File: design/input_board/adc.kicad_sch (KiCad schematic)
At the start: 8 parts, among them IC9 ADS8860IDGSR, U14 REF6050xDGK, U15 uA7805

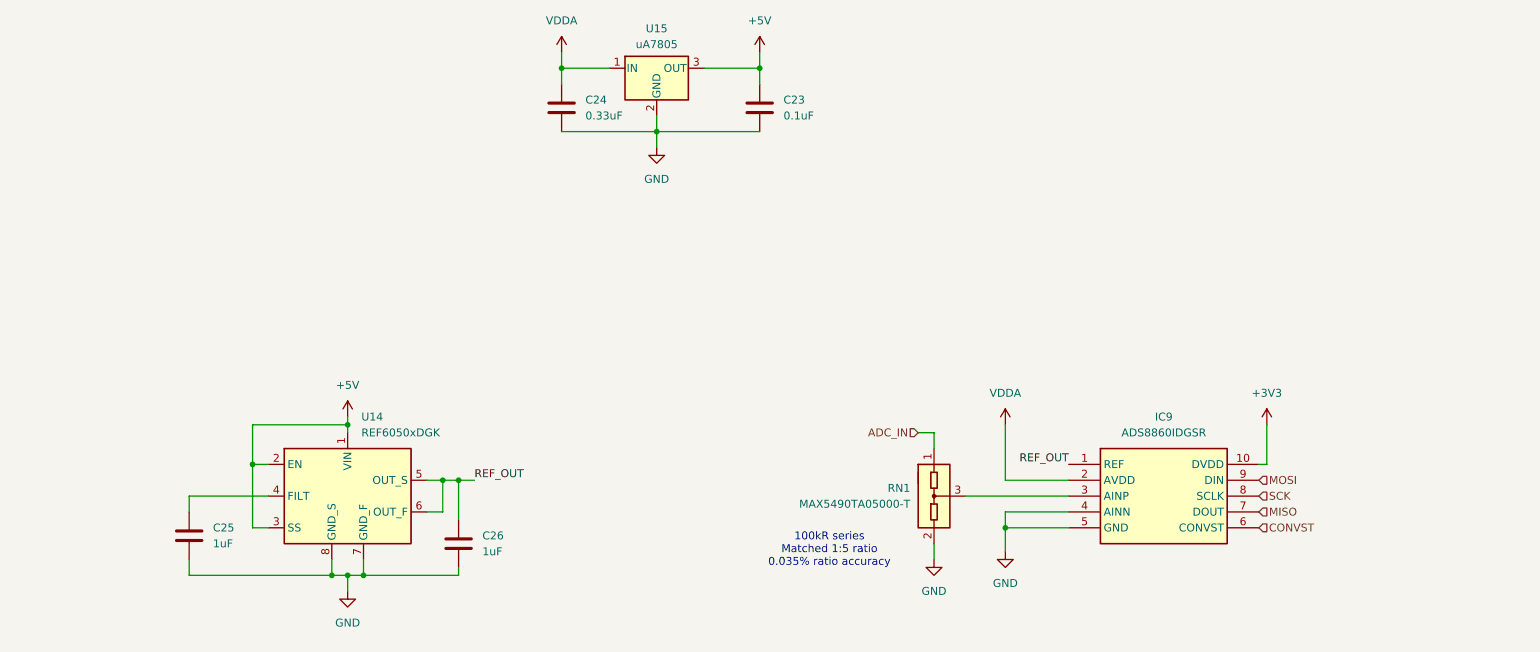
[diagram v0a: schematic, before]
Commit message: Finihs schamtic and footprints; DVDD 3.3->2V
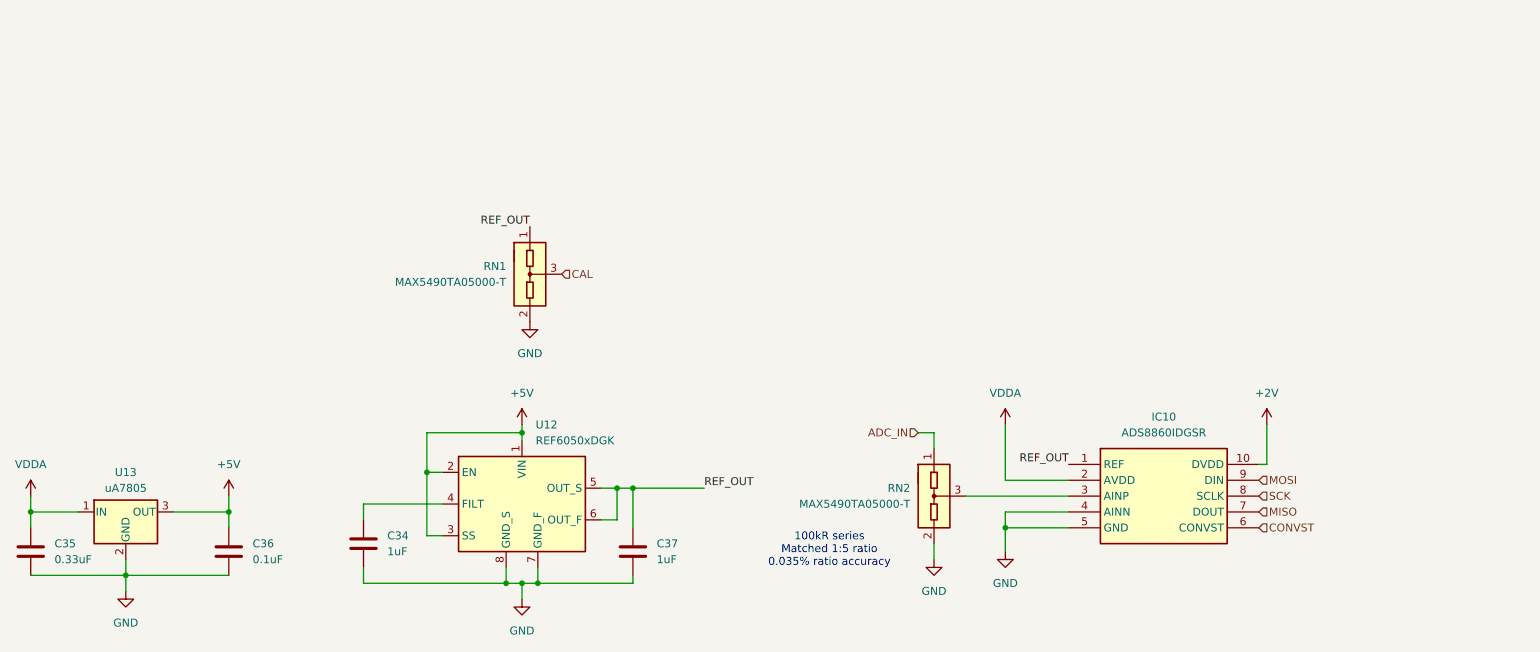
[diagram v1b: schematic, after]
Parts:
- added RN1: MAX5490TA05000-T, Package_TO_SOT_SMD:SOT-23, symbol input_board:MAX5490xxx-T
- C34: renamed from C25; footprint (none) -> Capacitor_SMD:C_0805_2012Metric_Pad1.18x1.45mm_HandSolder
- C35: renamed from C24; footprint (none) -> Capacitor_SMD:C_0805_2012Metric_Pad1.18x1.45mm_HandSolder
- C36: renamed from C23; footprint (none) -> Capacitor_SMD:C_0805_2012Metric_Pad1.18x1.45mm_HandSolder
- C37: renamed from C26; footprint (none) -> Capacitor_SMD:C_0805_2012Metric_Pad1.18x1.45mm_HandSolder
- U13: renamed from U15; footprint (none) -> Package_TO_SOT_SMD:TO-263-3_TabPin2
- renumbered IC9 to IC10, RN1 to RN2, U14 to U12
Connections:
- net GND: now also RN1.2 (R1)
- net REF_OUT: now also RN1.1 (COM1)
- net +3V3 renamed +2V
- new net CAL: RN1.3 (R2)
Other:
- moved on the sheet: C34, C35, C36, C37, U12, U13

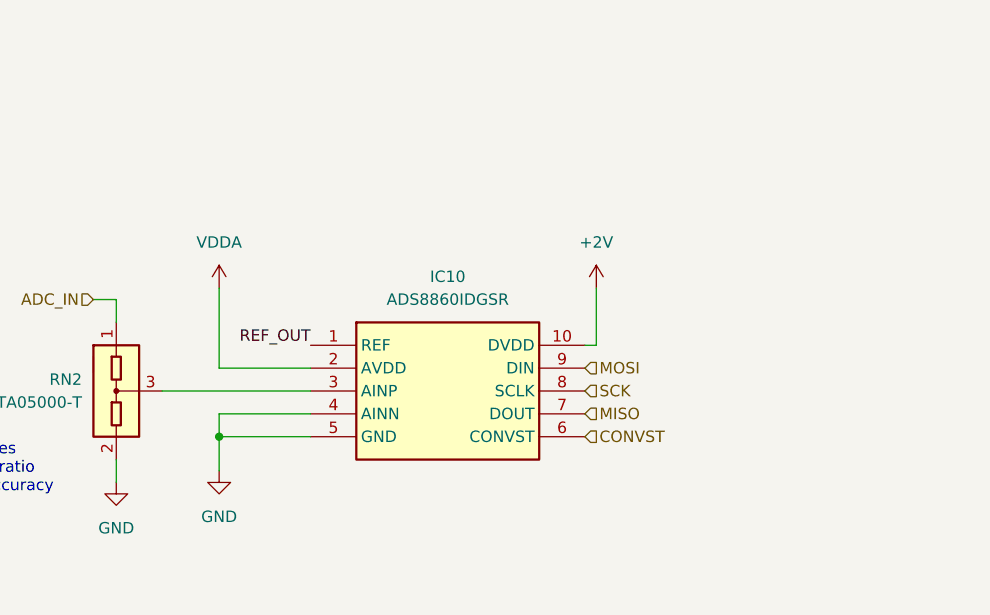
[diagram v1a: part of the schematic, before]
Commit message: Layout v1, its bad
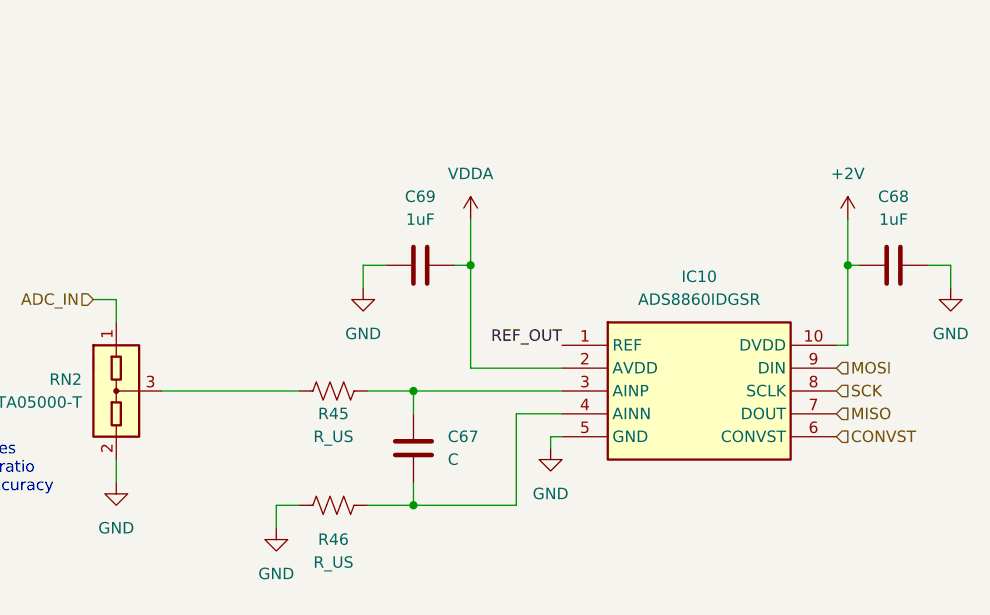
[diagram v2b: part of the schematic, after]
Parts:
- added C67: C, Capacitor_SMD:C_0805_2012Metric_Pad1.18x1.45mm_HandSolder, symbol Device:C
- added C68, C69: 1uF, Capacitor_SMD:C_0805_2012Metric_Pad1.18x1.45mm_HandSolder, symbol Device:C
- added R45, R46: R_US, Resistor_SMD:R_0805_2012Metric_Pad1.20x1.40mm_HandSolder, symbol Device:R_US
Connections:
- net +2V: now also C68.2
- net GND: now also C68.1, C69.1, R46.2; no longer IC10.4 (AINN)
- net VDDA: now also C69.2
- net at RN2.3 (R2): now also R45.1; no longer IC10.3 (AINP)
- new net: C67.2, IC10.3 (AINP), R45.2
- new net: C67.1, IC10.4 (AINN), R46.1
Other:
- moved on the sheet: IC10

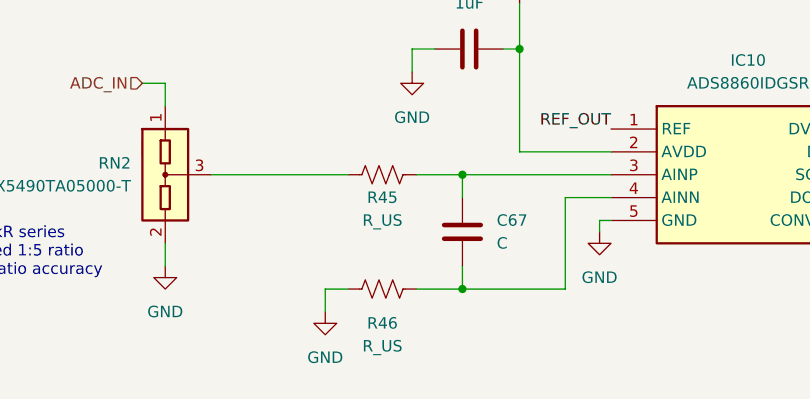
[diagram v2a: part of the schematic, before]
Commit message: Add values for charge bucket filter
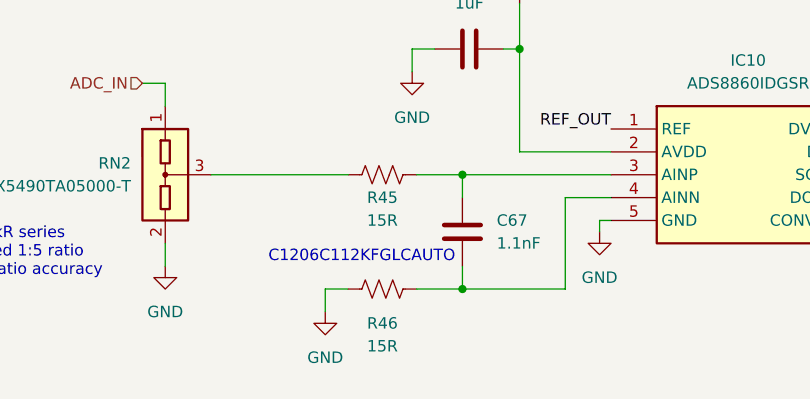
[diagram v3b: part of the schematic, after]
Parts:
- C67: value C -> 1.1nF
- R45, R46: value R_US -> 15R
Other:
- note added: "C1206C112KFGLCAUTO"
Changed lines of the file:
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@@
+		)
+	)
+	(text "C1206C112KFGLCAUTO"
+		(exclude_from_sim no)
+		(at 195.834 114.554 0)
+		(effects
+			(font
+				(size 1.27 1.27)
+			)
 		)
 	)
@@
 			)
 		)
-		(property "Value" "R_US"
+		(property "Value" "15R"
 			(at 198.12 110.49 90)
 			(effects
@@
 			)
 		)
-		(property "Value" "C"
+		(property "Value" "1.1nF"
 			(at 210.82 113.0299 0)
 			(effects
@@
 			)
 		)
-		(property "Value" "R_US"
+		(property "Value" "15R"
 			(at 198.12 124.46 90)
 			(effects
